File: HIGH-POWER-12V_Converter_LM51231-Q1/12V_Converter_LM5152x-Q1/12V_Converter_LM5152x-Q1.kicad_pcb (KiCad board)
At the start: 2 copper layers, 42.1 x 41.3 mm, 34 parts, among them M1 60V, M2 60V, U1 LM51521QRGRRQ1

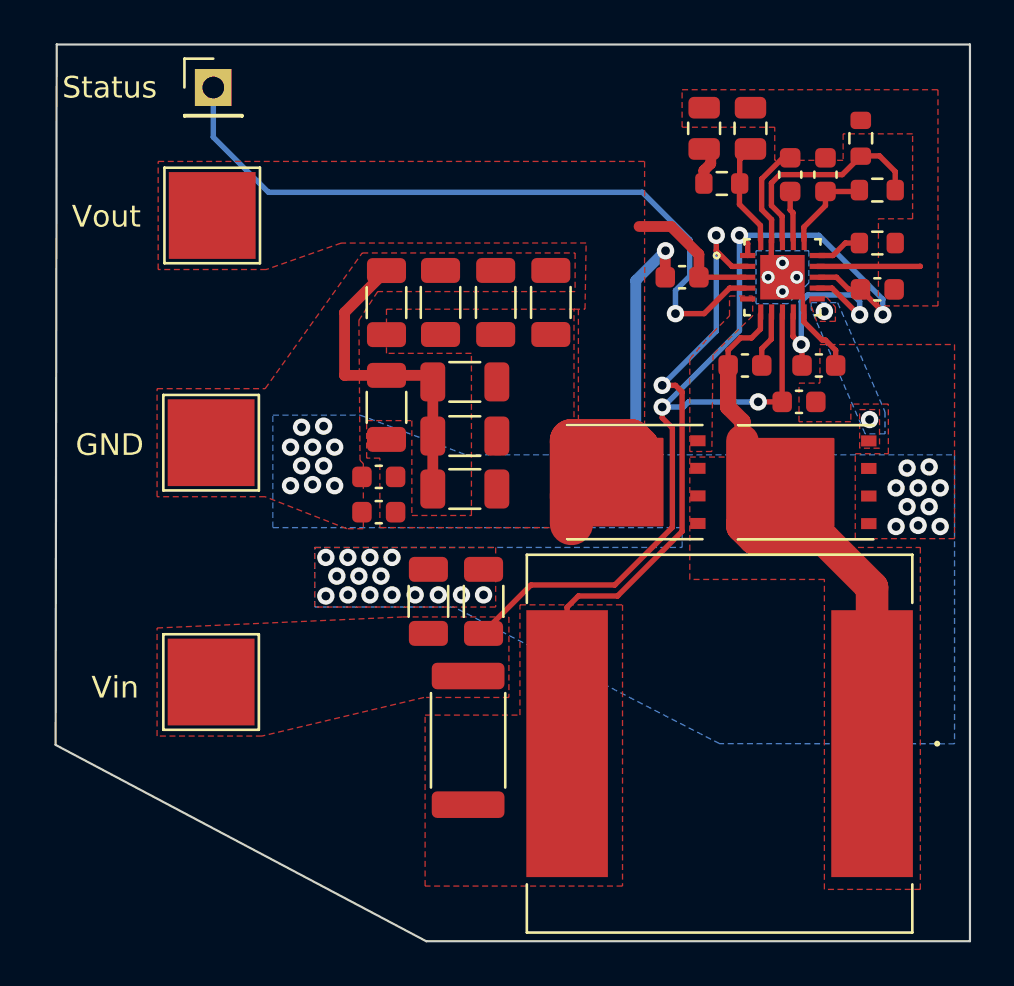
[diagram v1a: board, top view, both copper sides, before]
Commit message: updated current sense line
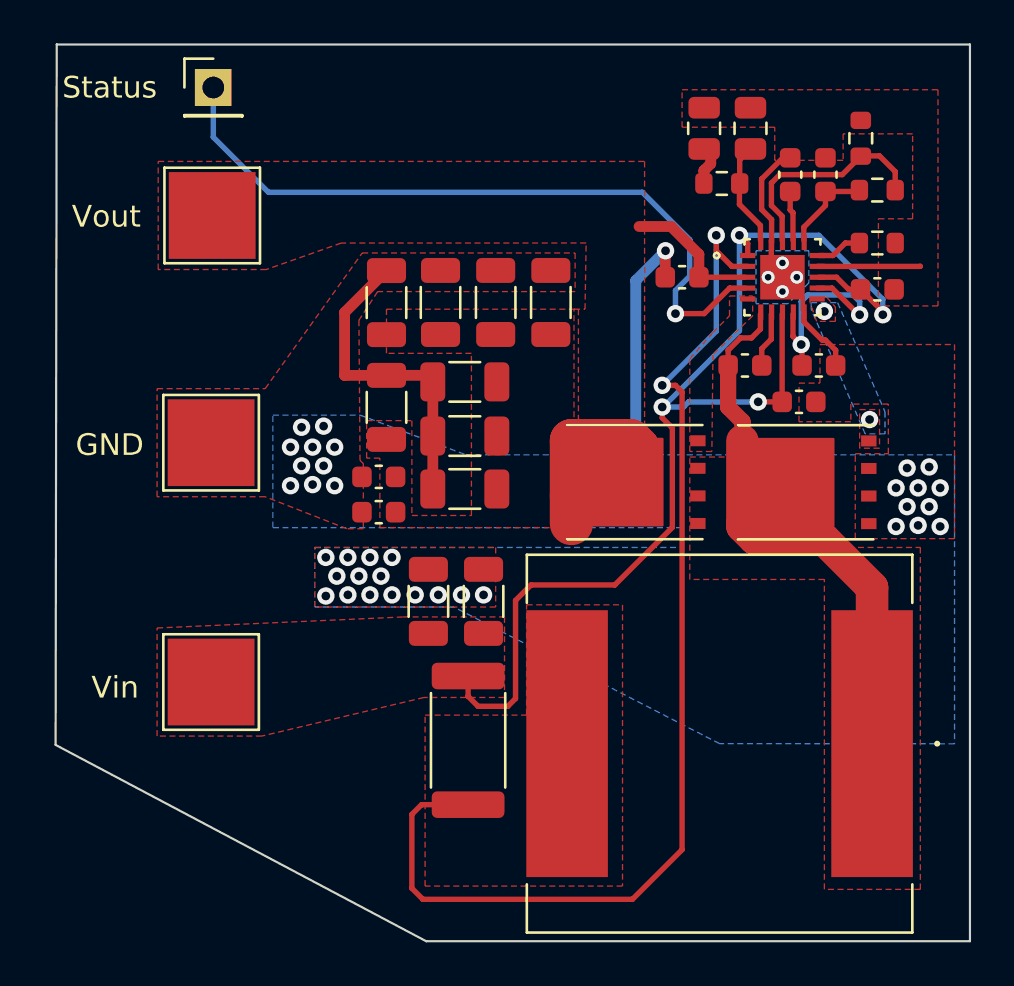
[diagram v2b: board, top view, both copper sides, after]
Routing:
- net Net-(L1-Pad2): track 30.9 -> 52.3 mm
- net Vin: track 48.9 -> 54.8 mm

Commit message: ngl idek
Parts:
- moved L1 0.51 mm to (98.6, 120.9)
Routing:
- net Net-(L1-Pad2): track 52.3 -> 36.8 mm
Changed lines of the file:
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@@
   )
   (footprint "inductor:HCMA1707-330-R" (layer "F.Cu")
-    (at 98.044 120.94845 180)
+    (at 98.552 120.94845 180)
     (property "Sheetfile" "12V_Converter_LM5152x-Q1.kicad_sch")
     (property "Sheetname" "")
@@
   (via (at 104.9528 106.0196) (size 0.8) (drill 0.4) (layers "F.Cu" "B.Cu") (free) (net 5))
   (via (at 102.87 101.0412) (size 0.8) (drill 0.4) (layers "F.Cu" "B.Cu") (free) (net 5))
+  (segment (start 99.6696 111.506) (end 102.8192 111.506) (width 1.5) (layer "F.Cu") (net 6))
   (segment (start 98.4374 103.5304) (end 98.4374 105.4478) (width 0.75) (layer "F.Cu") (net 6))
+  (segment (start 99.096401 110.81385) (end 99.096401 110.932801) (width 1.5) (layer "F.Cu") (net 6))
+  (segment (start 105.5751 120.44045) (end 105.0671 120.94845) (width 1.5) (layer "F.Cu") (net 6))
+  (segment (start 99.0092 102.2604) (end 98.4374 102.8322) (width 0.25) (layer "F.Cu") (net 6))
+  (segment (start 105.5751 114.2619) (end 105.5751 120.44045) (width 1.5) (layer "F.Cu") (net 6))
+  (segment (start 99.9241 101.16695) (end 99.9241 101.8535) (width 0.25) (layer "F.Cu") (net 6))
+  (segment (start 102.8192 111.506) (end 105.5751 114.2619) (width 1.5) (layer "F.Cu") (net 6))
   (segment (start 99.096401 110.932801) (end 99.6696 111.506) (width 1.5) (layer "F.Cu") (net 6))
-  (segment (start 99.0092 102.2604) (end 98.4374 102.8322) (width 0.25) (layer "F.Cu") (net 6))
-  (segment (start 102.8192 111.506) (end 105.0671 113.7539) (width 1.5) (layer "F.Cu") (net 6))
-  (segment (start 99.6696 111.506) (end 102.8192 111.506) (width 1.5) (layer "F.Cu") (net 6))
-  (segment (start 99.9241 101.16695) (end 99.9241 101.8535) (width 0.25) (layer "F.Cu") (net 6))
-  (segment (start 105.0671 113.7539) (end 105.0671 120.94845) (width 1.5) (layer "F.Cu") (net 6))
   (segment (start 99.096401 106.106801) (end 99.096401 107.00385) (width 0.75) (layer "F.Cu") (net 6))
-  (segment (start 99.096401 110.81385) (end 99.096401 110.932801) (width 1.5) (layer "F.Cu") (net 6))
   (segment (start 99.096401 107.00385) (end 99.096401 110.81385) (width 1.5) (layer "F.Cu") (net 6))
   (segment (start 98.4374 102.8322) (end 98.4374 103.5304) (width 0.25) (layer "F.Cu") (net 6))
@@
   (segment (start 101.924102 97.76585) (end 101.924102 97.161098) (width 0.25) (layer "F.Cu") (net 9))
   (segment (start 104.4196 95.517) (end 104.4834 95.4532) (width 0.25) (layer "F.Cu") (net 9))
-  (segment (start 96.3168 104.7496) (end 96.3168 125.8316) (width 0.25) (layer "F.Cu") (net 10))
+  (segment (start 98.610801 98.966401) (end 97.8916 98.2472) (width 0.25) (layer "F.Cu") (net 10))
+  (segment (start 96.012 104.4448) (end 96.3168 104.7496) (width 0.25) (layer "F.Cu") (net 10))
+  (segment (start 89.09552 119.28608) (end 86.4616 121.92) (width 0.25) (layer "F.Cu") (net 10))
+  (segment (start 93.396517 114.0968) (end 89.5604 114.0968) (width 0.25) (layer "F.Cu") (net 10))
+  (segment (start 99.3396 98.966401) (end 98.610801 98.966401) (width 0.25) (layer "F.Cu") (net 10))
   (segment (start 95.4024 104.4448) (end 96.012 104.4448) (width 0.25) (layer "F.Cu") (net 10))
-  (segment (start 98.610801 98.966401) (end 97.8916 98.2472) (width 0.25) (layer "F.Cu") (net 10))
-  (segment (start 83.8708 124.206) (end 84.31825 123.75855) (width 0.25) (layer "F.Cu") (net 10))
-  (segment (start 99.3396 98.966401) (end 98.610801 98.966401) (width 0.25) (layer "F.Cu") (net 10))
-  (segment (start 83.8708 127.6096) (end 83.8708 124.206) (width 0.25) (layer "F.Cu") (net 10))
-  (segment (start 84.31825 123.75855) (end 86.4616 123.75855) (width 0.25) (layer "F.Cu") (net 10))
+  (segment (start 89.5604 114.0968) (end 89.09552 114.56168) (width 0.25) (layer "F.Cu") (net 10))
   (segment (start 97.8916 98.2472) (end 97.8916 97.536) (width 0.25) (layer "F.Cu") (net 10))
-  (segment (start 96.3168 125.8316) (end 94.0308 128.1176) (width 0.25) (layer "F.Cu") (net 10))
-  (segment (start 96.012 104.4448) (end 96.3168 104.7496) (width 0.25) (layer "F.Cu") (net 10))
-  (segment (start 94.0308 128.1176) (end 84.3788 128.1176) (width 0.25) (layer "F.Cu") (net 10))
-  (segment (start 84.3788 128.1176) (end 83.8708 127.6096) (width 0.25) (layer "F.Cu") (net 10))
+  (segment (start 86.4616 121.92) (end 86.4616 123.75855) (width 0.25) (layer "F.Cu") (net 10))
+  (segment (start 89.09552 114.56168) (end 89.09552 119.28608) (width 0.25) (layer "F.Cu") (net 10))
+  (segment (start 96.3168 111.176517) (end 93.396517 114.0968) (width 0.25) (layer "F.Cu") (net 10))
+  (segment (start 96.3168 104.7496) (end 96.3168 111.176517) (width 0.25) (layer "F.Cu") (net 10))
   (via (at 97.8916 97.536) (size 0.8) (drill 0.4) (layers "F.Cu" "B.Cu") (free) (net 10))
   (via (at 95.4024 104.4448) (size 0.8) (drill 0.4) (layers "F.Cu" "B.Cu") (free) (net 10))
@@
         (xy 93.5736 127.508)
         (xy 84.4804 127.508)
-        (xy 84.4804 119.634)
-        (xy 89.154 119.634)
-        (xy 89.154 114.554)
+        (xy 84.4804 122.7328)
+        (xy 89.6112 122.7328)
+        (xy 89.6112 114.554)
         (xy 93.5736 114.554)
       )
